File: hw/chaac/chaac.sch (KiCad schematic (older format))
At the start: 53 parts, among them J1 Battery, J2 TC2030-CTX, J3 UART, J4 windrain, Q1 Q_PMOS_GSD, SW1 RST, SW2 RST, U1 TPS7A0530PDBVT, U2 NRF52811-QFAA, U3 BMP280, U4 SHT3x-DIS, U5 E22-X00M22S, Y2 32.768kHz

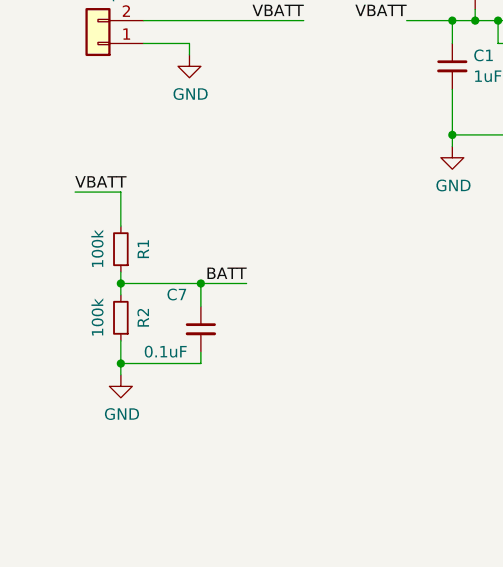
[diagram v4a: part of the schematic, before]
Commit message: Changing vbat sense resistors from 100k to 1Mohm
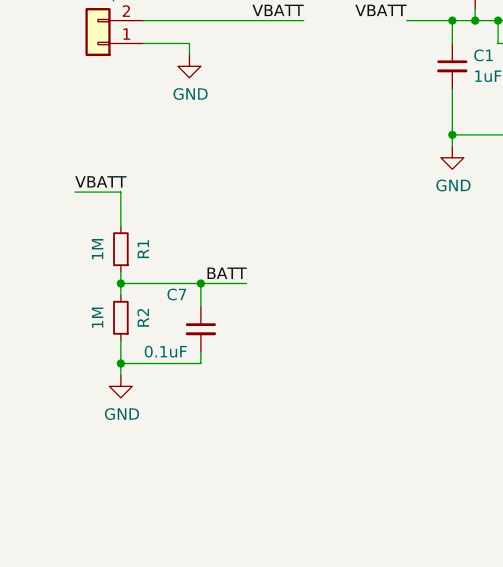
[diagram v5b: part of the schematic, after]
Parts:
- R1, R2: value 100k -> 1M; DKPN P100KGCT-ND -> P1.0MGCT-ND; MPN ERJ-3GEYJ104V -> ERJ-3GEYJ105V
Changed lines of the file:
@@
 Sheet 1 1
 Title "Chaac"
-Date "2020-06-16"
-Rev "4.0"
+Date "2020-07-19"
+Rev "4.1"
 Comp "@alvaroprieto"
 Comment1 ""
@@
 P 1450 2100
 F 0 "R1" V 1350 2100 50  0000 C CNN
-F 1 "100k" V 1550 2100 50  0000 C CNN
+F 1 "1M" V 1550 2100 50  0000 C CNN
 F 2 "Resistor_SMD:R_0603_1608Metric" H 1450 2100 50  0001 C CNN
 F 3 "~" H 1450 2100 50  0001 C CNN
-F 4 "P100KGCT-ND" H 450 1150 50  0001 C CNN "DKPN"
-F 5 " ERJ-3GEYJ104V " H 450 1150 50  0001 C CNN "MPN"
+F 4 "P1.0MGCT-ND" H 450 1150 50  0001 C CNN "DKPN"
+F 5 "ERJ-3GEYJ105V" H 450 1150 50  0001 C CNN "MPN"
 	1    1450 2100
 	-1   0    0    1
@@
 P 1450 2400
 F 0 "R2" V 1350 2400 50  0000 C CNN
-F 1 "100k" V 1550 2400 50  0000 C CNN
+F 1 "1M" V 1550 2400 50  0000 C CNN
 F 2 "Resistor_SMD:R_0603_1608Metric" H 1450 2400 50  0001 C CNN
 F 3 "~" H 1450 2400 50  0001 C CNN
-F 4 "P100KGCT-ND" H 450 1150 50  0001 C CNN "DKPN"
-F 5 " ERJ-3GEYJ104V " H 450 1150 50  0001 C CNN "MPN"
+F 4 "P1.0MGCT-ND" H 450 1150 50  0001 C CNN "DKPN"
+F 5 "ERJ-3GEYJ105V" H 450 1150 50  0001 C CNN "MPN"
 	1    1450 2400
 	-1   0    0    1

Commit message: Adding chaac v5.0
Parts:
- removed C1: 1uF, Capacitor_SMD:C_0603_1608Metric, symbol Device:C_Small
- removed C14: 0.1uF, Capacitor_SMD:C_0603_1608Metric, symbol Device:C_Small
- removed J3: UART, Connector_PinHeader_2.54mm:PinHeader_1x03_P2.54mm_Vertical, symbol Connector_Generic:Conn_01x03
- removed R14, R6: 4.7k, Resistor_SMD:R_0603_1608Metric, symbol Device:R_Small
- removed SW1, SW2: RST, alvarop:PTS820J25MSMTRLFS, symbol Switch:SW_Push
- removed U3: BMP280, alvarop:BMP280, symbol alvarop:BMP280
- added C1: 100uF, Capacitor_SMD:CP_Elec_6.3x5.4, symbol Device:CP_Small
- added C2: 10uF, Resistor_SMD:R_0603_1608Metric, symbol Device:C_Small
- added C3, C8: 4.7uF, Capacitor_SMD:C_0402_1005Metric, symbol Device:C_Small
- added C7: 0.1uF, Capacitor_SMD:C_0402_1005Metric, symbol Device:C_Small
- added D1: RB521CS30L,315, alvarop:RB521CS30L, symbol Device:D_Schottky_Small_ALT
- added D2, D3, D4: LED_ALT, LED_SMD:LED_0603_1608Metric, symbol Device:LED_ALT
- added J2: Battery, alvarop:S2B-PH-SM4-TB, symbol Connector_Generic:Conn_01x02
- added J3: UART, Connector_PinHeader_2.54mm:PinHeader_1x02_P2.54mm_Vertical, symbol Connector_Generic:Conn_01x02
- added R1: 270k, Resistor_SMD:R_0402_1005Metric, symbol Device:R_Small
- added R10, R11, R12, R13, R20: 10k, Resistor_SMD:R_0402_1005Metric, symbol Device:R_Small
- added R2, R5: 100k, Resistor_SMD:R_0402_1005Metric, symbol Device:R_Small
- added R4: 1M, Resistor_SMD:R_0402_1005Metric, symbol Device:R_Small
- added U2: MCP73871, alvarop:MCP73871, symbol Battery_Management:MCP73871
- added U4: DPS368, alvarop:DPS368, symbol alvarop:DPS368
- C10: renamed from C4; DKPN 490-5915-1-ND -> 1276-1482-1-ND; MPN GRM155R60J475ME47D -> CL05A475MP5NRNC
- C18: renamed from C17; footprint Capacitor_SMD:C_0603_1608Metric -> Capacitor_SMD:C_0402_1005Metric; DKPN 311-1085-1-ND -> 1276-1028-1-ND; MPN CC0603KRX7R9BB103 -> CL05B103KB5NNNC
- C19: renamed from C18; footprint Capacitor_SMD:C_0603_1608Metric -> Capacitor_SMD:C_0402_1005Metric; DKPN 311-1085-1-ND -> 1276-1028-1-ND; MPN CC0603KRX7R9BB103 -> CL05B103KB5NNNC
- C20: renamed from C15; footprint Capacitor_SMD:C_0603_1608Metric -> Capacitor_SMD:C_0402_1005Metric; DKPN 490-1532-1-ND -> 490-1318-1-ND; MPN GRM188R71C104KA01D -> GRM155R61A104KA01D
- C21: renamed from C16; footprint Capacitor_SMD:C_0603_1608Metric -> Capacitor_SMD:C_0402_1005Metric; DKPN 490-1532-1-ND -> 490-1318-1-ND; MPN GRM188R71C104KA01D -> GRM155R61A104KA01D
- C22: renamed from C21; footprint Capacitor_SMD:C_0603_1608Metric -> Capacitor_SMD:C_0402_1005Metric; DKPN 490-1532-1-ND -> 490-1318-1-ND; MPN GRM188R71C104KA01D -> GRM155R61A104KA01D
- C23: renamed from C22; footprint Capacitor_SMD:C_0603_1608Metric -> Capacitor_SMD:C_0402_1005Metric; DKPN 490-1536-1-ND -> 445-175218-1-ND; MPN GRM188R61C105KA93D -> C1005X5R1V105K050BE
- C24: renamed from C19; footprint Capacitor_SMD:C_0603_1608Metric -> Capacitor_SMD:C_0402_1005Metric; DKPN 490-1532-1-ND -> 490-1318-1-ND; MPN GRM188R71C104KA01D -> GRM155R61A104KA01D
- C25: renamed from C20; footprint Capacitor_SMD:C_0603_1608Metric -> Capacitor_SMD:C_0402_1005Metric; DKPN 490-1532-1-ND -> 490-1318-1-ND; MPN GRM188R71C104KA01D -> GRM155R61A104KA01D
- C5: renamed from C2; footprint Capacitor_SMD:C_0603_1608Metric -> Capacitor_SMD:C_0402_1005Metric; DKPN 490-1536-1-ND -> 445-175218-1-ND; MPN GRM188R61C105KA93D -> C1005X5R1V105K050BE
- C6: renamed from C7; footprint Capacitor_SMD:C_0603_1608Metric -> Capacitor_SMD:C_0402_1005Metric; DKPN 490-1532-1-ND -> 490-1318-1-ND; MPN GRM188R71C104KA01D -> GRM155R61A104KA01D
- C9: renamed from C3; DKPN 311-1438-1-ND -> 445-175218-1-ND; MPN CC0402KRX5R5BB105 -> C1005X5R1V105K050BE
- J1: value Battery -> Solar
- R14: renamed from R3; footprint Resistor_SMD:R_0603_1608Metric -> Resistor_SMD:R_0402_1005Metric; DKPN 311-10.0KHRCT-ND -> 311-10KJRCT-ND; MPN RC0603FR-0710KL -> RC0402JR-0710KL
- R15: renamed from R4; footprint Resistor_SMD:R_0603_1608Metric -> Resistor_SMD:R_0402_1005Metric; DKPN 311-10.0KHRCT-ND -> 311-10KJRCT-ND; MPN RC0603FR-0710KL -> RC0402JR-0710KL
- R16: renamed from R10; value 1k -> 0; footprint Resistor_SMD:R_0603_1608Metric -> Resistor_SMD:R_0402_1005Metric; DKPN 311-1.00KHRCT-ND -> (none); MPN RC0603FR-071KL -> (none)
- R17: renamed from R11; footprint Resistor_SMD:R_0603_1608Metric -> Resistor_SMD:R_0402_1005Metric; DKPN 311-1.00KHRCT-ND -> A106129CT-ND; MPN RC0603FR-071KL -> CRG0402J1K0
- R18: renamed from R12; footprint Resistor_SMD:R_0603_1608Metric -> Resistor_SMD:R_0402_1005Metric; DKPN 311-1.00KHRCT-ND -> A106129CT-ND; MPN RC0603FR-071KL -> CRG0402J1K0
- R19: renamed from R13; footprint Resistor_SMD:R_0603_1608Metric -> Resistor_SMD:R_0402_1005Metric; DKPN 311-1.00KHRCT-ND -> A106129CT-ND; MPN RC0603FR-071KL -> CRG0402J1K0
- R21: renamed from R5; footprint Resistor_SMD:R_0603_1608Metric -> Resistor_SMD:R_0402_1005Metric; DKPN 311-10.0KHRCT-ND -> 311-10KJRCT-ND; MPN RC0603FR-0710KL -> RC0402JR-0710KL
- R22: renamed from R15; footprint Resistor_SMD:R_0603_1608Metric -> Resistor_SMD:R_0402_1005Metric; DKPN 311-1.00KHRCT-ND -> A106129CT-ND; MPN RC0603FR-071KL -> CRG0402J1K0
- R23: renamed from R16; footprint Resistor_SMD:R_0603_1608Metric -> Resistor_SMD:R_0402_1005Metric; DKPN 311-1.00KHRCT-ND -> A106129CT-ND; MPN RC0603FR-071KL -> CRG0402J1K0
- R3: renamed from R1; footprint Resistor_SMD:R_0603_1608Metric -> Resistor_SMD:R_0402_1005Metric; DKPN P1.0MGCT-ND -> 541-3965-1-ND; MPN ERJ-3GEYJ105V -> CRCW04021M00FKEDC
- R6: renamed from R2; footprint Resistor_SMD:R_0603_1608Metric -> Resistor_SMD:R_0402_1005Metric; DKPN P1.0MGCT-ND -> 541-3965-1-ND; MPN ERJ-3GEYJ105V -> CRCW04021M00FKEDC
- R7: value 4.7k -> 1M; footprint Resistor_SMD:R_0603_1608Metric -> Resistor_SMD:R_0402_1005Metric; DKPN 311-4.7KGRCT-ND -> 541-3965-1-ND; MPN RC0603JR-074K7L -> CRCW04021M00FKEDC
- R8: value 0 -> 100k; footprint Resistor_SMD:R_0603_1608Metric -> Resistor_SMD:R_0402_1005Metric; DKPN 311-0.0GRCT-ND -> 311-100KLRCT-ND; MPN RC0603JR-070RL -> RC0402FR-07100KL
- R9: value DNP -> 1M; footprint Resistor_SMD:R_0603_1608Metric -> Resistor_SMD:R_0402_1005Metric; DKPN (none) -> 541-3965-1-ND; MPN (none) -> CRCW04021M00FKEDC
- Y1: renamed from Y2; footprint Crystal:Crystal_SMD_3215-2Pin_3.2x1.5mm -> alvarop:ABS05; DKPN ‎SER4084CT-ND‎ -> 535-11897-1-ND; MPN FC-135 32.7680KA-AC0 -> ABS05-32.768KHZ-9-T
- renumbered C5 to C11, C6 to C12, C9 to C13, C11 to C14, C12 to C15, C13 to C17, D1 to D5, D2 to D6, J2 to J4, J4 to J5, U2 to U3, U4 to U5, U5 to U6
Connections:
- net labels added: MCP_VIN, SOLAR_IN, VIN, VSOLAR
- net labels removed: BOOT, UART_RX
- wire segments 280 -> 332
- no-connect marks 21 -> 23
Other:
- note added: "4.5V VPCC Setting"
- note added: "7-bit I2C Addr: 0x76\n"
- note added: "Charge Current\n1000V/(20mA) = 50kOhm"
- note added: "Termination Current\n1000V/(1mA) = 1MOhm"
- note added: "Using internal pull-up\nfor I2C (100kHz only!)"
- note removed: "7-bit I2C Addr: 0x76"
- moved on the sheet: C10, C11, C12, C13, C14, C15, C17, C20, C21, C22, C23, C5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

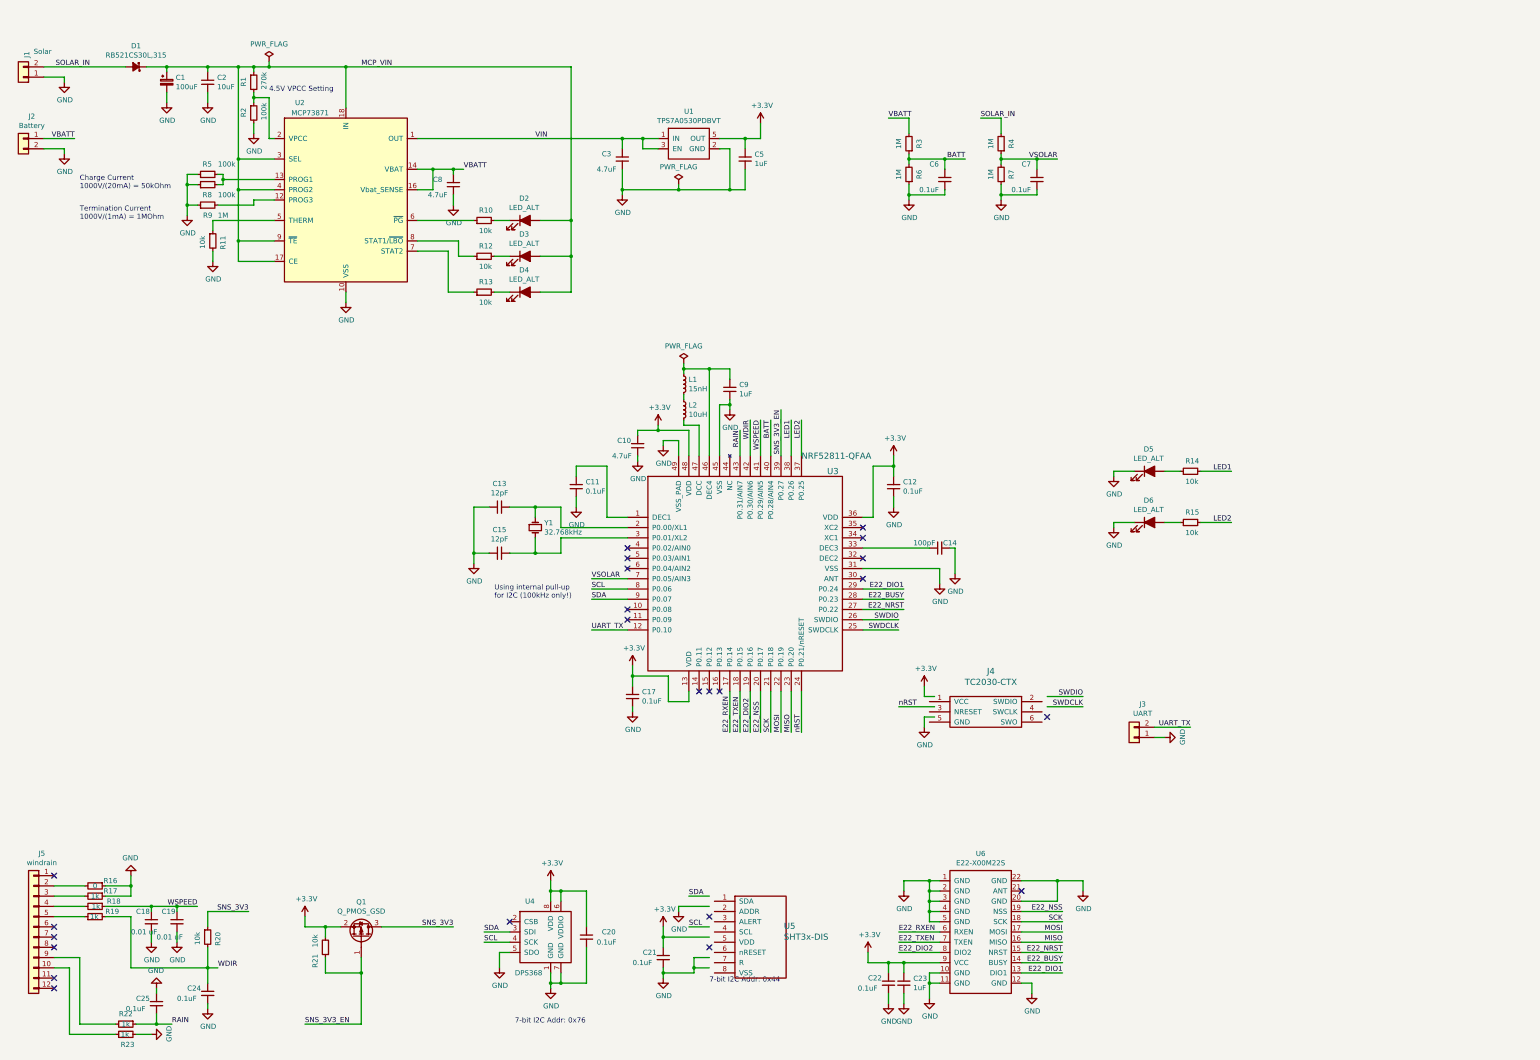
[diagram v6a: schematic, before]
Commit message: Re-did layout for chaac v6
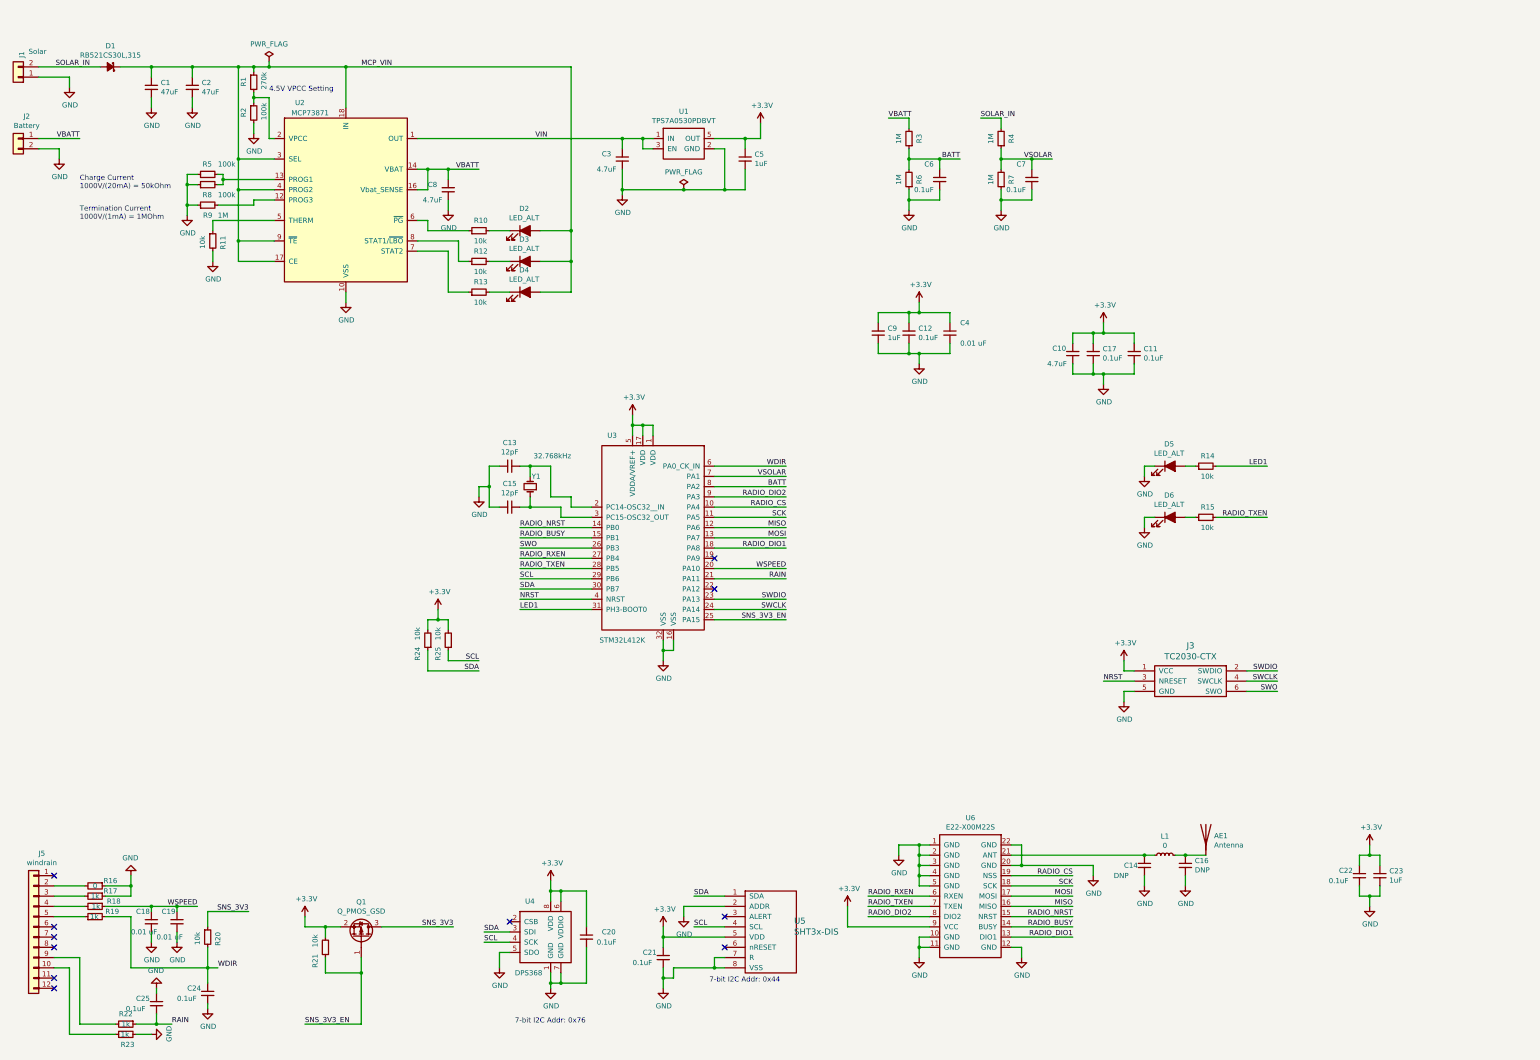
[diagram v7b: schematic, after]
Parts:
- removed C1: 100uF, Capacitor_SMD:CP_Elec_6.3x5.4, symbol Device:CP_Small
- removed J3: UART, Connector_PinHeader_2.54mm:PinHeader_1x02_P2.54mm_Vertical, symbol Connector_Generic:Conn_01x02
- removed J4: TC2030-CTX, alvarop:TC2030-NL, symbol alvarop:TC2030-CTX
- removed L2: 10uH, Inductor_SMD:L_0603_1608Metric, symbol Device:L_Small
- removed U3: NRF52811-QFAA, alvarop:NRF52811-QFN48-VIAS, symbol alvarop:NRF52811-QFAA
- added AE1: Antenna, alvarop:ANT-916-HESM, symbol Device:Antenna
- added C1: 47uF, Capacitor_SMD:C_1206_3216Metric, symbol Device:C_Small
- added C16: DNP, Capacitor_SMD:C_0402_1005Metric, symbol Device:C_Small
- added C4: 0.01 uF, Capacitor_SMD:C_0402_1005Metric, symbol Device:C_Small
- added J3: TC2030-CTX, alvarop:TC2030-NL, symbol alvarop:TC2030-CTX
- added R24, R25: 10k, Resistor_SMD:R_0402_1005Metric, symbol Device:R_Small
- added U3: STM32L412K, alvarop:UFQFPN32, symbol alvarop:STM32L412K
- C14: value 100pF -> DNP; DKPN 587-1211-1-ND -> (none); MPN UMK105CG101JV-F -> (none)
- C2: value 10uF -> 47uF; footprint Resistor_SMD:R_0603_1608Metric -> Capacitor_SMD:C_1206_3216Metric; DKPN 1276-1192-1-ND -> (none); MPN CL10A106KP8NNNC -> (none)
- L1: value 15nH -> 0; DKPN 587-1521-1-ND‎ -> (none); MPN HK100515NJ-T‎ -> (none)
- U6: MPN E22-X00M22S -> (none)
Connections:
- net labels added: NRST, RADIO_BUSY, RADIO_CS, RADIO_DIO1, RADIO_DIO2, RADIO_NRST, RADIO_RXEN, RADIO_TXEN, SWCLK, SWO
- net labels removed: E22_BUSY, E22_DIO1, E22_DIO2, E22_NRST, E22_NSS, E22_RXEN, E22_TXEN, LED2, SWDCLK, UART_TX, nRST
- wire segments 332 -> 347
- no-connect marks 23 -> 11
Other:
- note removed: "Using internal pull-up\nfor I2C (100kHz only!)"
- moved on the sheet: C10, C11, C12, C13, C15, C17, C22, C23, C6, C7, C8, C9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

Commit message: Cleaned up chaac layout
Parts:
- U3: footprint alvarop:UFQFPN32 -> alvarop:UFQFPN32_ALT
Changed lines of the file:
@@
 F 0 "U3" H 6900 7300 50  0000 C CNN
 F 1 "STM32L412K" H 7000 5300 50  0000 C CNN
-F 2 "alvarop:UFQFPN32" V 6800 6100 50  0001 C CNN
+F 2 "alvarop:UFQFPN32_ALT" V 6800 6100 50  0001 C CNN
 F 3 "" V 6800 6100 50  0001 C CNN
 	1    7300 6100
